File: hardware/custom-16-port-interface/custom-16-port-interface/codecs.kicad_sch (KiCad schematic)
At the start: 92 parts

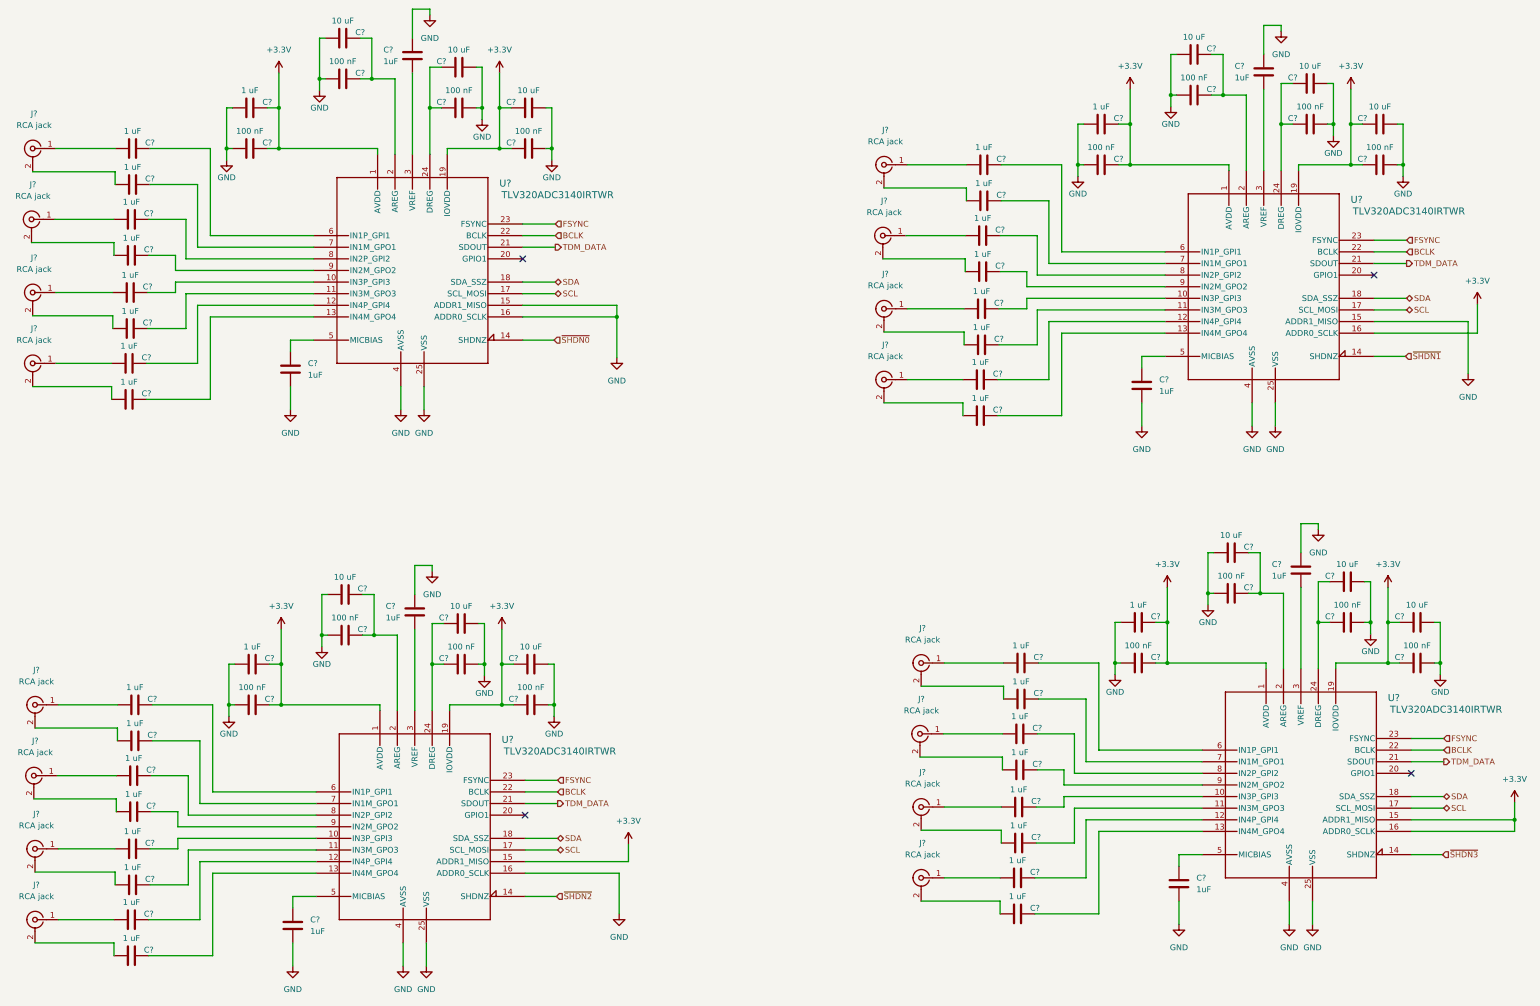
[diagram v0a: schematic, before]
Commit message: Added fpga firmware for ADAT->TDM, updated schematic
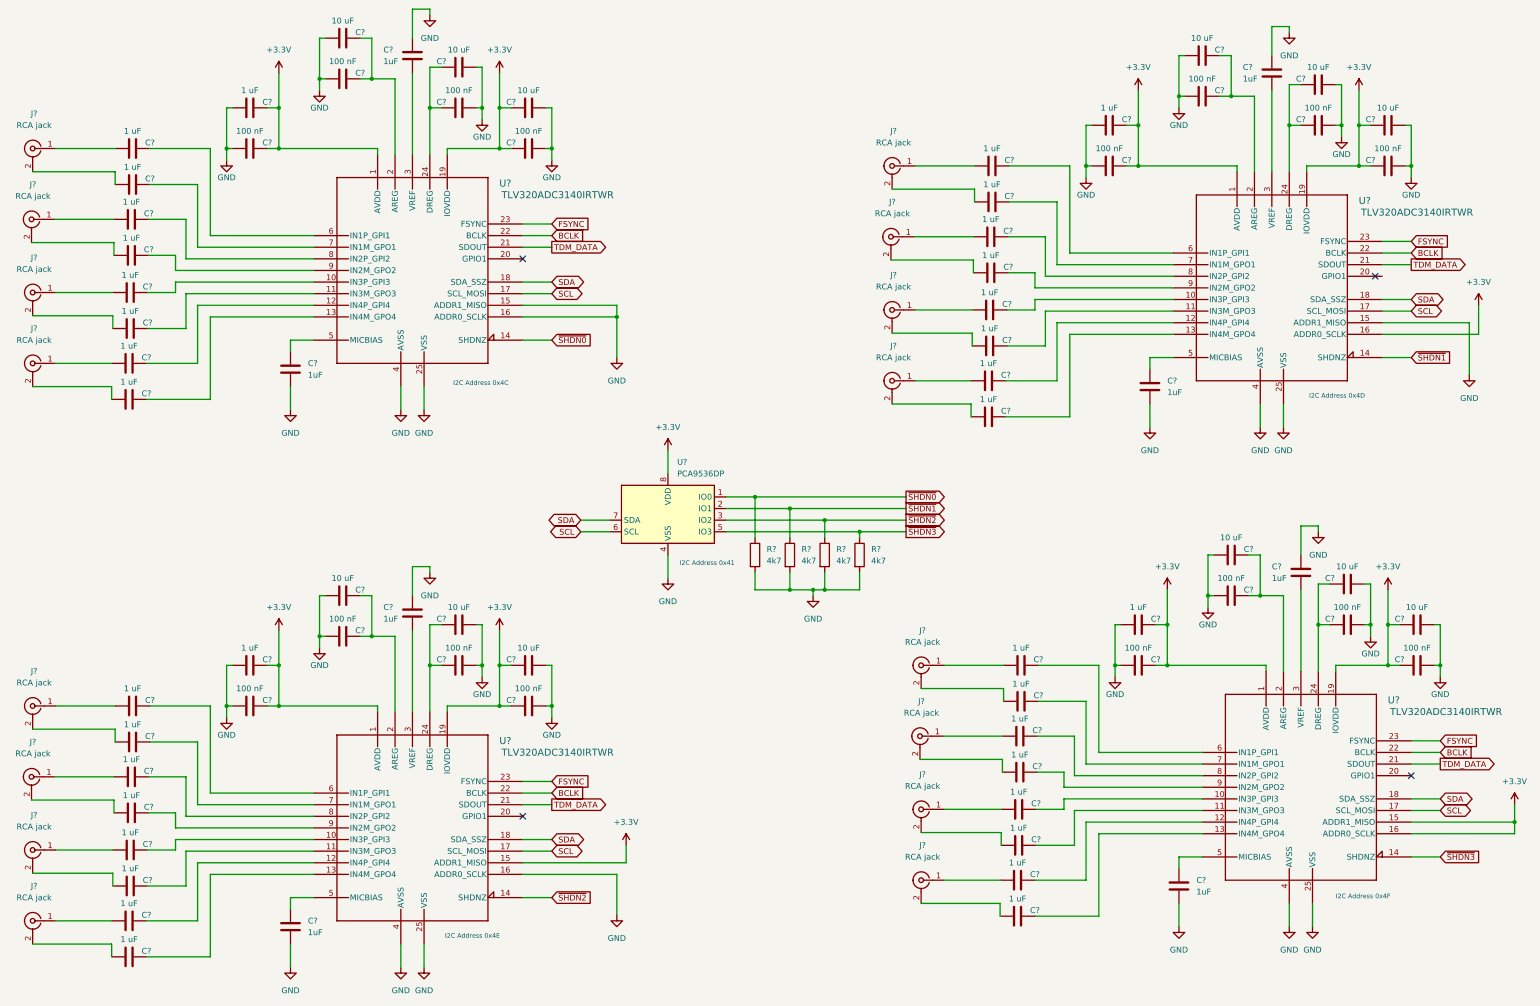
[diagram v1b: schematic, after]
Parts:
- added R? (x4): 4k7, symbol Device:R
- added U?: PCA9536DP, Package_SO:TSSOP-8_3x3mm_P0.65mm, symbol Interface_Expansion:PCA9536DP
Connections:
- net +3.3V: now also U?.8 (VDD)
- net GND: now also R?.2, R?.2, R?.2, R?.2, U?.4 (VSS)
- net SCL: now also U?.6 (SCL)
- net SDA: now also U?.7 (SDA)
- net ~{SHDN0}: now also R?.1, U?.1 (IO0)
- net ~{SHDN1}: now also R?.1, U?.2 (IO1)
- net ~{SHDN2}: now also R?.1, U?.3 (IO2)
- net ~{SHDN3}: now also R?.1, U?.5 (IO3)
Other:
- note added: "I2C Address 0x41"
- note added: "I2C Address 0x4C"
- note added: "I2C Address 0x4D"
- note added: "I2C Address 0x4E"
- note added: "I2C Address 0x4F"
- moved on the sheet: C?, J?, U?
